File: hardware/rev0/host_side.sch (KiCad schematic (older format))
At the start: 9 parts, among them IC1 ECP5-BGA256, U11 USB3343

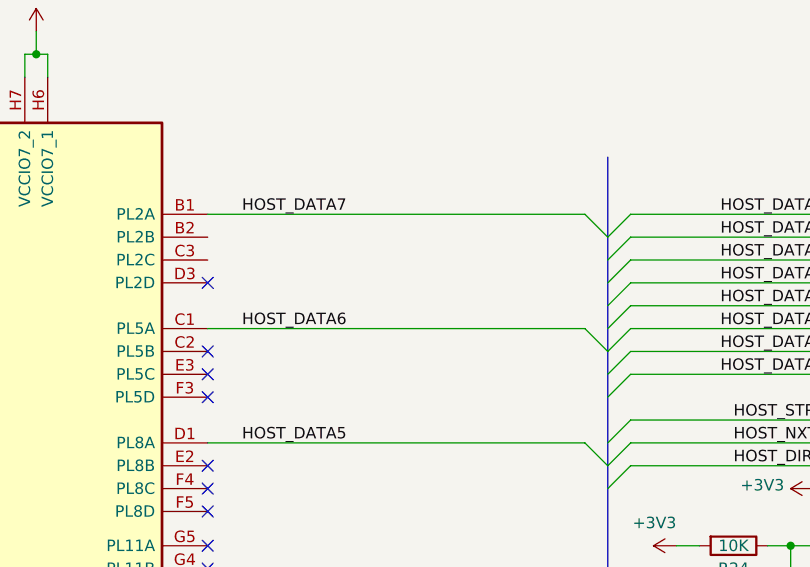
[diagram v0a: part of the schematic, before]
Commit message: Start re-arranging user IO
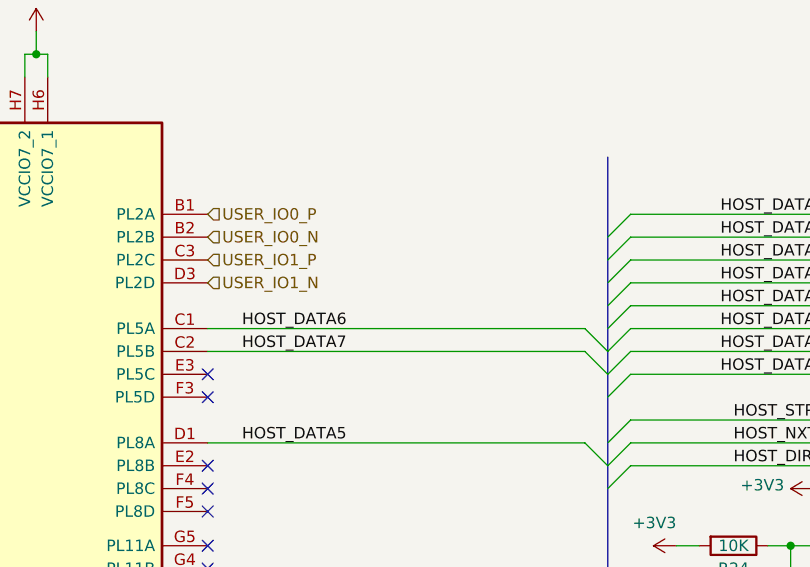
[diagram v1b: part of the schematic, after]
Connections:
- net HOST_DATA7: now also IC1.C2 (PL5B); no longer IC1.B1 (PL2A)
- net USER_IO0_N: now reaches IC1.B2 (PL2B)
- net USER_IO1_P: now reaches IC1.C3 (PL2C)
- net USER_IO1_N: now reaches IC1.D3 (PL2D)
- new net USER_IO0_P: IC1.B1 (PL2A)
- no-connect marks 18 -> 16
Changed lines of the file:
@@
 	5150 3350 5250 3350
 Connection ~ 5250 3350
-NoConn ~ 2700 2200
-NoConn ~ 2700 2500
 NoConn ~ 2700 2600
 NoConn ~ 2700 2700
@@
 HOST_DATA6
 Wire Wire Line
-	2700 1900 4350 1900
+	2700 2500 4350 2500
 Entry Wire Line
-	4350 1900 4450 2000
+	4350 2500 4450 2600
 Entry Wire Line
 	4350 3650 4450 3750
-Text Label 2850 1900 0    50   ~ 0
+Text Label 2850 2500 0    50   ~ 0
 HOST_DATA7
 $Comp
@@
 Wire Bus Line
 	4450 1650 4450 5800
+Text HLabel 2700 1900 2    50   Input ~ 0
+USER_IO0_P
+Text HLabel 2700 2000 2    50   Input ~ 0
+USER_IO0_N
+Text HLabel 2700 2200 2    50   Input ~ 0
+USER_IO1_N
+Text HLabel 2700 2100 2    50   Input ~ 0
+USER_IO1_P
 $EndSCHEMATC

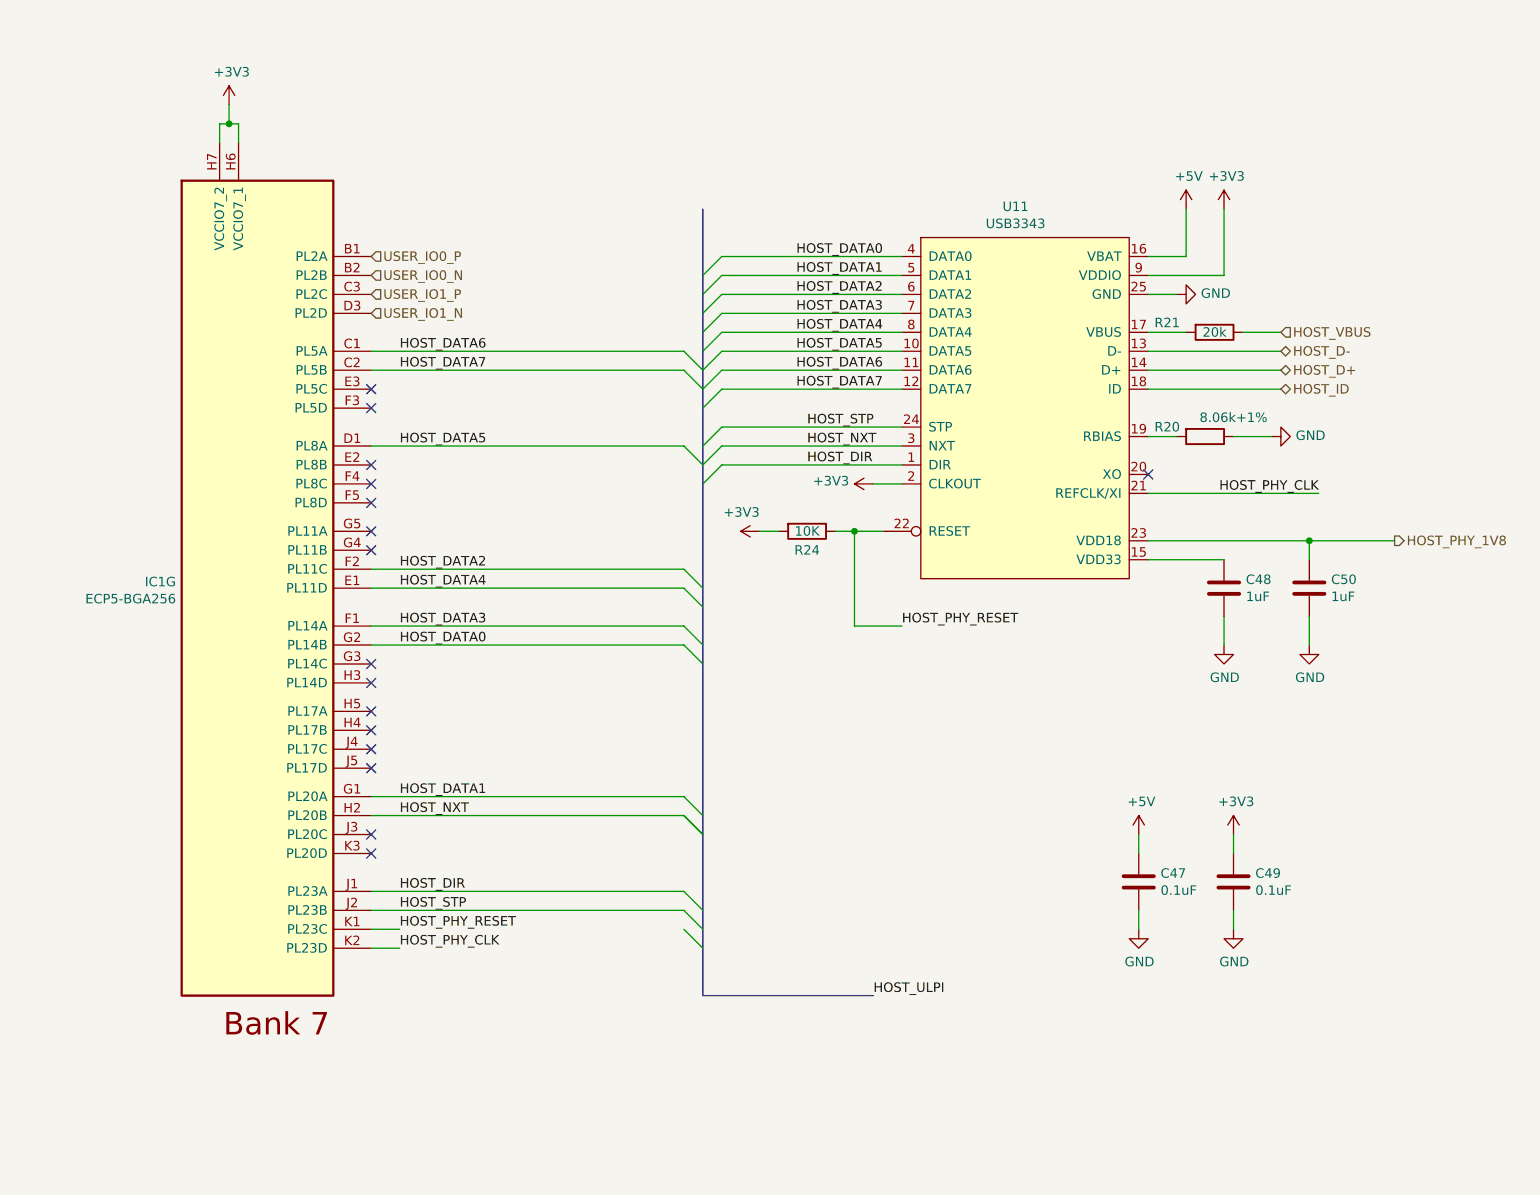
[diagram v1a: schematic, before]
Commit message: Route LVDS user IO
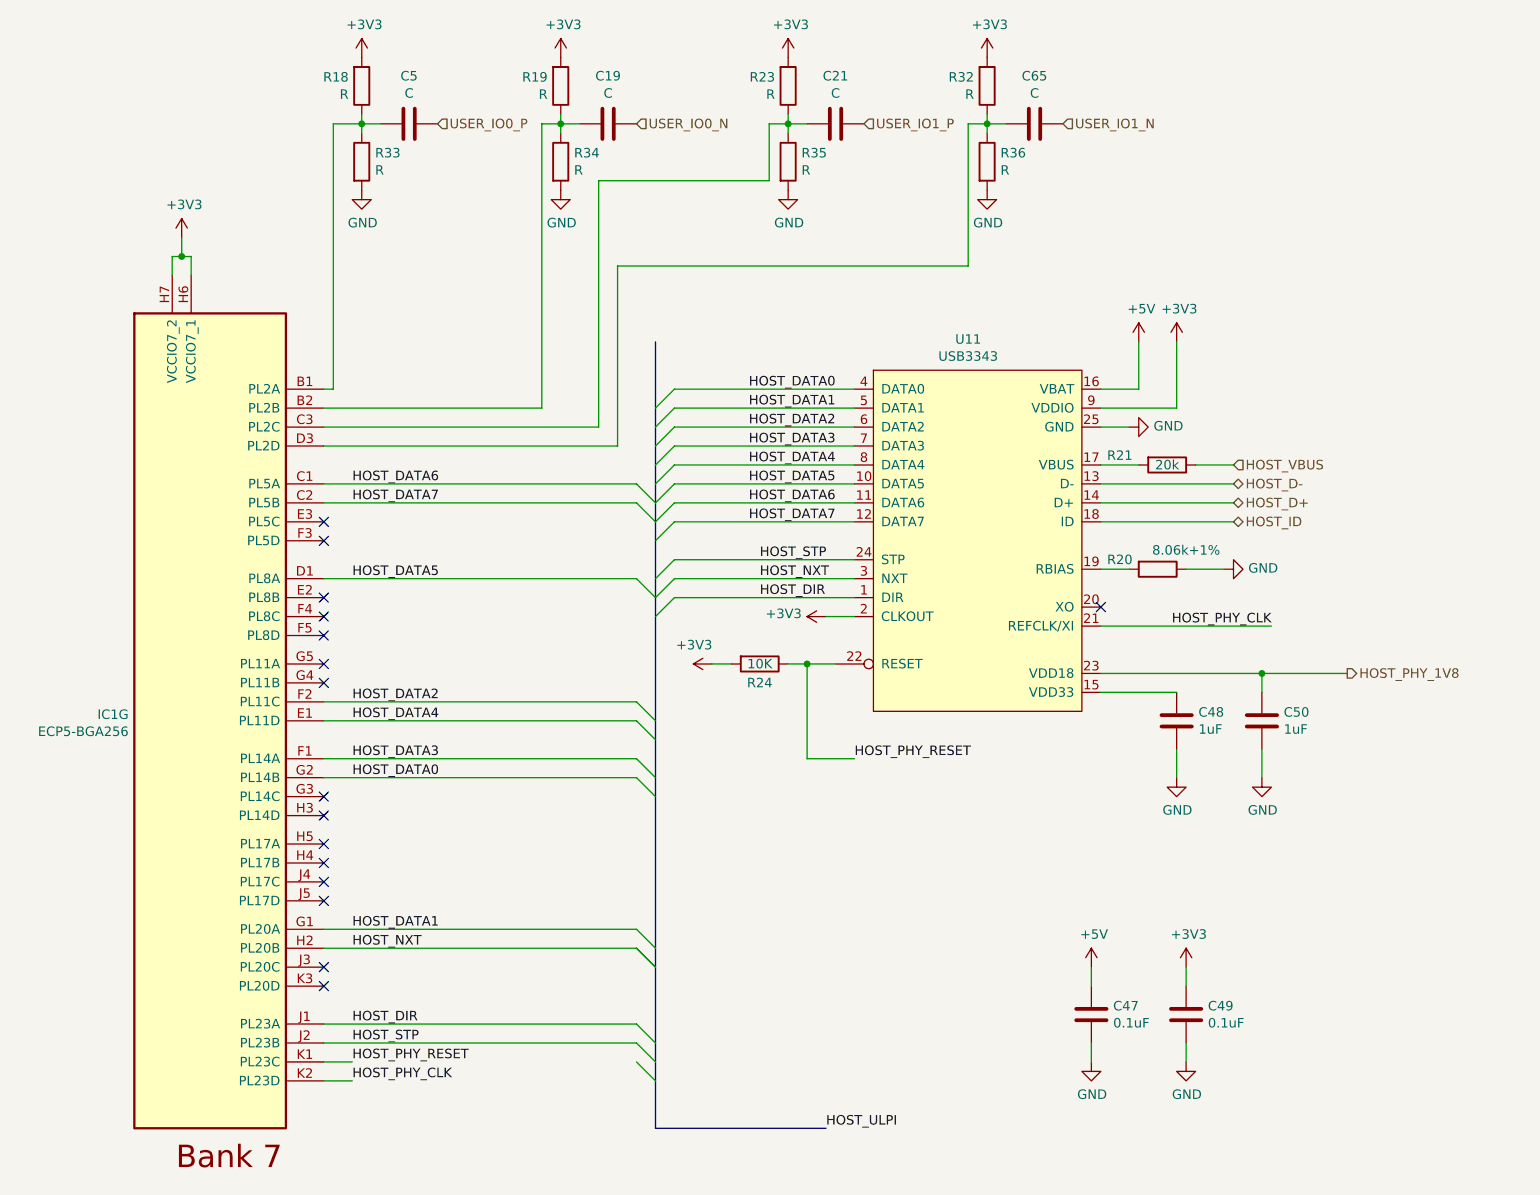
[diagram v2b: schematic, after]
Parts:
- added C19, C21, C5, C65: C, Capacitor_SMD:C_0402_1005Metric, symbol Device:C
- added R18, R19, R23, R32, R33, R34, R35, R36: R, Resistor_SMD:R_0402_1005Metric, symbol Device:R
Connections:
- net +3V3: now also R18.2, R19.2, R23.2, R32.2
- net GND: now also R33.2, R34.2, R35.2, R36.2
- net USER_IO0_N: now also C19.1; no longer IC1.B2 (PL2B)
- net USER_IO0_P: now also C5.1; no longer IC1.B1 (PL2A)
- net USER_IO1_N: now also C65.1; no longer IC1.D3 (PL2D)
- net USER_IO1_P: now also C21.1; no longer IC1.C3 (PL2C)
- new net: C5.2, IC1.B1 (PL2A), R18.1, R33.1
- new net: C19.2, IC1.B2 (PL2B), R19.1, R34.1
- new net: C21.2, IC1.C3 (PL2C), R23.1, R35.1
- new net: C65.2, IC1.D3 (PL2D), R32.1, R36.1
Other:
- moved on the sheet: C47, C48, C49, C50, IC1G, R20, R21, R24, U11

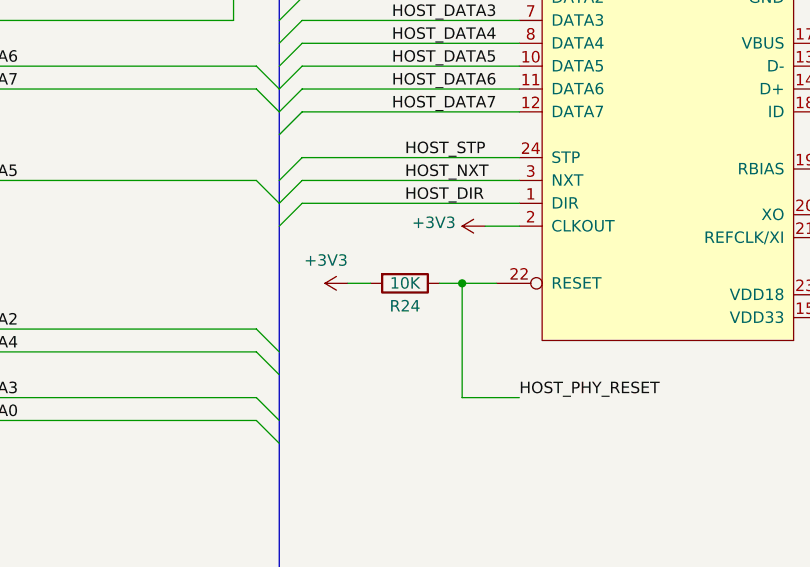
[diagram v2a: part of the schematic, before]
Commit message: Tidy up component values
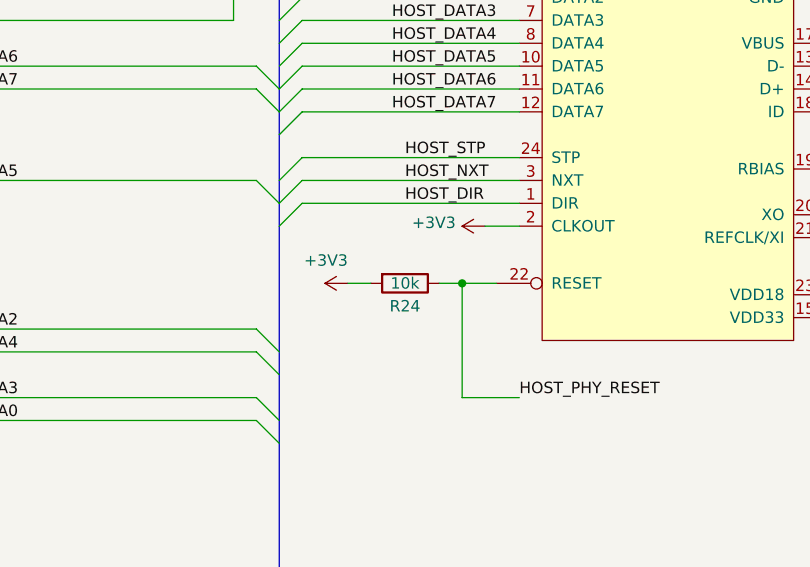
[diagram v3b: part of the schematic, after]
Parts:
- R24: value 10K -> 10k
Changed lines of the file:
@@
 P 4750 4050
 F 0 "R24" V 4850 4050 50  0000 C CNN
-F 1 "10K" V 4750 4050 50  0000 C CNN
+F 1 "10k" V 4750 4050 50  0000 C CNN
 F 2 "Resistor_SMD:R_0402_1005Metric" V 4680 4050 50  0001 C CNN
 F 3 "~" H 4750 4050 50  0001 C CNN

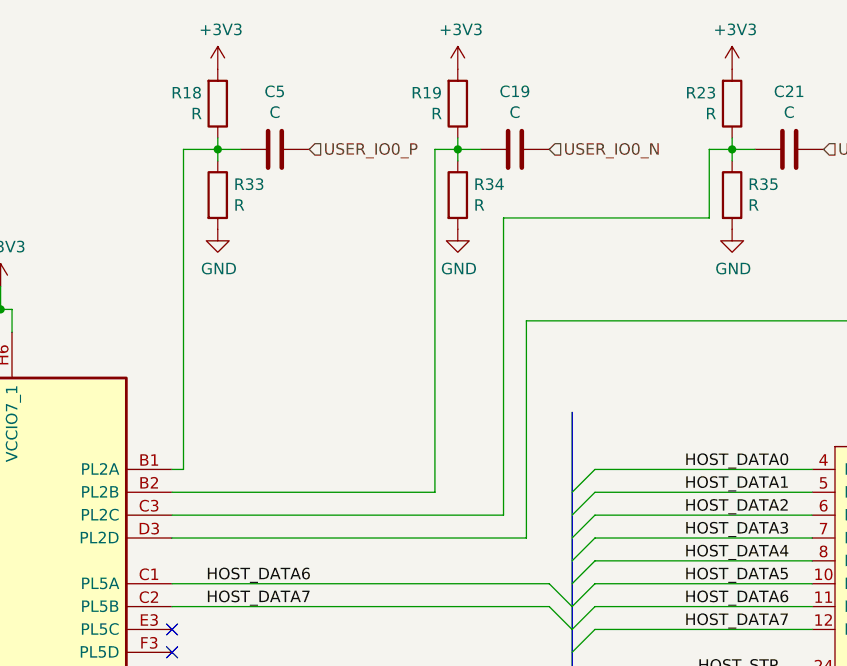
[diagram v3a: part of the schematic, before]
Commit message: Rejig user IO
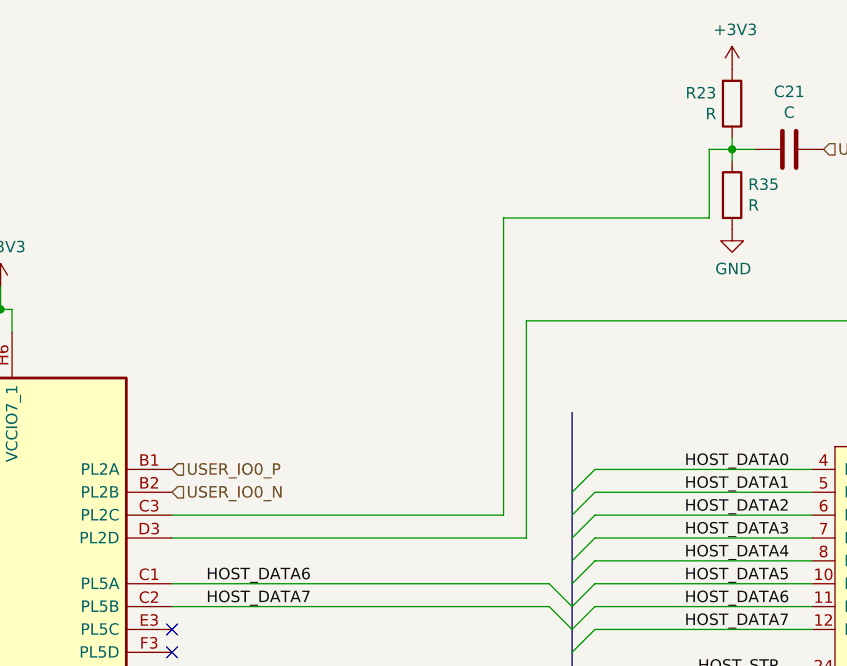
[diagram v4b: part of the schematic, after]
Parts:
- removed C19, C5: C, Capacitor_SMD:C_0402_1005Metric, symbol Device:C
- removed R18, R19, R33, R34: R, Resistor_SMD:R_0402_1005Metric, symbol Device:R
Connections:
- net USER_IO0_N: now also IC1.B2 (PL2B)
- net USER_IO0_P: now also IC1.B1 (PL2A)
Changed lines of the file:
@@
 Wire Wire Line
 	6550 4200 6950 4200
-Text HLabel 3050 1200 2    50   Input ~ 0
+Text HLabel 2450 2600 2    50   Input ~ 0
 USER_IO0_P
-Text HLabel 4100 1200 2    50   Input ~ 0
+Text HLabel 2450 2700 2    50   Input ~ 0
 USER_IO0_N
 Text HLabel 6350 1200 2    50   Input ~ 0
@@
 Text HLabel 5300 1200 2    50   Input ~ 0
 USER_IO1_P
-$Comp
-L Device:C C5
-U 1 1 5EB25D60
-P 2900 1200
-F 0 "C5" V 2648 1200 50  0000 C CNN
-F 1 "C" V 2739 1200 50  0000 C CNN
-F 2 "Capacitor_SMD:C_0402_1005Metric" H 2938 1050 50  0001 C CNN
-F 3 "~" H 2900 1200 50  0001 C CNN
-	1    2900 1200
-	0    1    1    0
-$EndComp
-$Comp
-L Device:R R33
-U 1 1 5EB266BA
-P 2650 1400
-F 0 "R33" H 2720 1446 50  0000 L CNN
-F 1 "R" H 2720 1355 50  0000 L CNN
-F 2 "Resistor_SMD:R_0402_1005Metric" V 2580 1400 50  0001 C CNN
-F 3 "~" H 2650 1400 50  0001 C CNN
-	1    2650 1400
-	1    0    0    -1
-$EndComp
-$Comp
-L Device:R R18
-U 1 1 5EB273F4
-P 2650 1000
-F 0 "R18" H 2581 954 50  0000 R CNN
-F 1 "R" H 2581 1045 50  0000 R CNN
-F 2 "Resistor_SMD:R_0402_1005Metric" V 2580 1000 50  0001 C CNN
-F 3 "~" H 2650 1000 50  0001 C CNN
-	1    2650 1000
-	1    0    0    1
-$EndComp
-$Comp
-L power:GND #PWR0110
-U 1 1 5EB283AE
-P 2650 1550
-F 0 "#PWR0110" H 2650 1300 50  0001 C CNN
-F 1 "GND" H 2655 1377 50  0000 C CNN
-F 2 "" H 2650 1550 50  0001 C CNN
-F 3 "" H 2650 1550 50  0001 C CNN
-	1    2650 1550
-	1    0    0    -1
-$EndComp
-Wire Wire Line
-	2650 1150 2650 1200
-Wire Wire Line
-	2650 1200 2750 1200
-Connection ~ 2650 1200
-Wire Wire Line
-	2650 1200 2650 1250
-$Comp
-L Device:C C19
-U 1 1 5EB3EF37
-P 3950 1200
-F 0 "C19" V 3698 1200 50  0000 C CNN
-F 1 "C" V 3789 1200 50  0000 C CNN
-F 2 "Capacitor_SMD:C_0402_1005Metric" H 3988 1050 50  0001 C CNN
-F 3 "~" H 3950 1200 50  0001 C CNN
-	1    3950 1200
-	0    1    1    0
-$EndComp
-$Comp
-L Device:R R34
-U 1 1 5EB3EF41
-P 3700 1400
-F 0 "R34" H 3770 1446 50  0000 L CNN
-F 1 "R" H 3770 1355 50  0000 L CNN
-F 2 "Resistor_SMD:R_0402_1005Metric" V 3630 1400 50  0001 C CNN
-F 3 "~" H 3700 1400 50  0001 C CNN
-	1    3700 1400
-	1    0    0    -1
-$EndComp
-$Comp
-L Device:R R19
-U 1 1 5EB3EF4B
-P 3700 1000
-F 0 "R19" H 3631 954 50  0000 R CNN
-F 1 "R" H 3631 1045 50  0000 R CNN
-F 2 "Resistor_SMD:R_0402_1005Metric" V 3630 1000 50  0001 C CNN
-F 3 "~" H 3700 1000 50  0001 C CNN
-	1    3700 1000
-	1    0    0    1
-$EndComp
-$Comp
-L power:GND #PWR0111
-U 1 1 5EB3EF5F
-P 3700 1550
-F 0 "#PWR0111" H 3700 1300 50  0001 C CNN
-F 1 "GND" H 3705 1377 50  0000 C CNN
-F 2 "" H 3700 1550 50  0001 C CNN
-F 3 "" H 3700 1550 50  0001 C CNN
-	1    3700 1550
-	1    0    0    -1
-$EndComp
-Wire Wire Line
-	3700 1150 3700 1200
-Wire Wire Line
-	3700 1200 3800 1200
-Connection ~ 3700 1200
-Wire Wire Line
-	3700 1200 3700 1250
 $Comp
 L Device:C C21
@@
 	5950 1200 5950 1250
 Wire Wire Line
-	2450 2600 2500 2600
-Wire Wire Line
-	2500 2600 2500 1200
-Wire Wire Line
-	2500 1200 2650 1200
-Wire Wire Line
-	2450 2700 3600 2700
-Wire Wire Line
-	3600 2700 3600 1200
-Wire Wire Line
-	3600 1200 3700 1200
-Wire Wire Line
 	2450 2800 3900 2800
 Wire Wire Line
@@
 	5850 1200 5950 1200
 $Comp
-L power:+3V3 #PWR0138
-U 1 1 5EBC52B8
-P 2650 850
-F 0 "#PWR0138" H 2650 700 50  0001 C CNN
-F 1 "+3V3" H 2664 1023 50  0000 C CNN
-F 2 "" H 2650 850 50  0001 C CNN
-F 3 "" H 2650 850 50  0001 C CNN
-	1    2650 850
-	1    0    0    -1
-$EndComp
-$Comp
-L power:+3V3 #PWR0139
-U 1 1 5EBC5820
-P 3700 850
-F 0 "#PWR0139" H 3700 700 50  0001 C CNN
-F 1 "+3V3" H 3714 1023 50  0000 C CNN
-F 2 "" H 3700 850 50  0001 C CNN
-F 3 "" H 3700 850 50  0001 C CNN
-	1    3700 850
-	1    0    0    -1
-$EndComp
-$Comp
 L power:+3V3 #PWR0140

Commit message: Pick part numbers for BOM
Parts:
- C47, C49: Manufacturer_Part_Number (none) -> LMF105B7104KVHF
- C48, C50: Manufacturer_Part_Number (none) -> LMK107B7225KA-T
- R20: Manufacturer_Part_Number (none) -> CRCW04028K06FKED
- R21: Manufacturer_Part_Number (none) -> CRCW040220K0FKEDC
- R24: Manufacturer_Part_Number (none) -> CRCW040210K0FKEDC
- U11: Manufacturer_Part_Number (none) -> USB3343-CP-TR
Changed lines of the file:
@@
 F 2 "Resistor_SMD:R_0402_1005Metric" V 6830 3000 50  0001 C CNN
 F 3 "~" H 6900 3000 50  0001 C CNN
+F 4 "CRCW040220K0FKEDC" H 6900 3000 50  0001 C CNN "Manufacturer_Part_Number"
 	1    6900 3000
 	0    1    1    0
@@
 F 2 "Resistor_SMD:R_0402_1005Metric" V 6780 3550 50  0001 C CNN
 F 3 "~" H 6850 3550 50  0001 C CNN
+F 4 "CRCW04028K06FKED" H 6850 3550 50  0001 C CNN "Manufacturer_Part_Number"
 	1    6850 3550
 	0    1    1    0
@@
 F 2 "Capacitor_SMD:C_0603_1608Metric" H 7438 4200 50  0001 C CNN
 F 3 "~" H 7400 4350 50  0001 C CNN
+F 4 "LMK107B7225KA-T" H 7400 4350 50  0001 C CNN "Manufacturer_Part_Number"
 	1    7400 4350
 	1    0    0    -1
@@
 F 2 "Capacitor_SMD:C_0603_1608Metric" H 6988 4200 50  0001 C CNN
 F 3 "~" H 6950 4350 50  0001 C CNN
+F 4 "LMK107B7225KA-T" H 6950 4350 50  0001 C CNN "Manufacturer_Part_Number"
 	1    6950 4350
 	1    0    0    -1
@@
 F 2 "Capacitor_SMD:C_0402_1005Metric" H 6538 5750 50  0001 C CNN
 F 3 "~" H 6500 5900 50  0001 C CNN
+F 4 "LMF105B7104KVHF" H 6500 5900 50  0001 C CNN "Manufacturer_Part_Number"
 	1    6500 5900
 	1    0    0    -1
@@
 F 2 "Capacitor_SMD:C_0402_1005Metric" H 7038 5750 50  0001 C CNN
 F 3 "~" H 7000 5900 50  0001 C CNN
+F 4 "LMF105B7104KVHF" H 7000 5900 50  0001 C CNN "Manufacturer_Part_Number"
 	1    7000 5900
 	1    0    0    -1
@@
 F 2 "Resistor_SMD:R_0402_1005Metric" V 4680 4050 50  0001 C CNN
 F 3 "~" H 4750 4050 50  0001 C CNN
+F 4 "CRCW040210K0FKEDC" H 4750 4050 50  0001 C CNN "Manufacturer_Part_Number"
 	1    4750 4050
 	0    1    1    0
@@
 F 2 "Package_DFN_QFN:VQFN-24-1EP_4x4mm_P0.5mm_EP2.45x2.45mm" H 5250 2500 50  0001 C CNN
 F 3 "http://ww1.microchip.com/downloads/en/DeviceDoc/334x.pdf" H 5250 2500 50  0001 C CNN
+F 4 "USB3343-CP-TR" H 5250 2500 50  0001 C CNN "Manufacturer_Part_Number"
 	1    5250 2500
 	1    0    0    -1
